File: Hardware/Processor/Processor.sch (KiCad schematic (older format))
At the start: 0 parts

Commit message: Started schematic capture for mcu dev board
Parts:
- added C? (x2): 10uF, symbol C
- added C?: 22uF, symbol C
- added C? (x17): 100nF, symbol C
- added C? (x7): 10nF, symbol C
- added C?: 4.7uF, symbol C
- added C?: 2.2uF, symbol C
- added D?: Zener, symbol D_Zener_ALT
- added J?: SWD, symbol CONN_02X05
- added L?: 2.2uH, symbol L
- added L?: 10uH, symbol L
- added R? (x3): 100k, symbol R
- added R?: 1R, symbol R
- added R?: 10k, symbol R
- added U?: ATSAM4E16E, symbol ATSAM4E16E
- added U?: TPS62162, symbol TPS6216
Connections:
- net labels added: +1V2, +3V3, +5V, AREF, GND, SWDCLK, SWDIO, TRACESWO, VDDPLL, ~P_GOOD, ~RST
- wire segments 0 -> 147
- no-connect marks 0 -> 3

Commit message: Changed buck regulator, added usb hw, added pio busses & net names
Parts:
- removed R?: 100k, symbol R
- removed U?: TPS62162, symbol TPS6216
- added C?: 4.5nF, symbol C
- added J?: USB_OTG, symbol USB_OTG
- added R?: 1M, symbol R
- added R? (x2): 0R, symbol R
- added TVS?: PRTR5V0U2X, symbol PRTR5V0U2X
- added U?: LM3671, symbol LM3671
- C?: value 10uF -> 4.7uF
- C?: value 22uF -> 10uF
- D?: value Zener -> 3.0V
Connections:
- net labels added: DD+, DD-, ERASE, PA0, PA1, PA10, PA11, PA12, PA13, PA14, PA15, PA16, PA17, PA18, PA19, PA2, PA20, PA21, PA22, PA23, PA24, PA25, PA26, PA27, PA28, PA29, PA3, PA30, PA31, PA4, PA5, PA6, PA7, PA8, PA9, PB0, PB1, PB13, PB14, PB2, PB3, PB4, PB5, PB6, PB7, PC0, PC1, PC10, PC11, PC12, PC13, PC14, PC15, PC16, PC17, PC18, PC19, PC2, PC20, PC21, PC22, PC23, PC24, PC25, PC26, PC27, PC28, PC29, PC3, PC30, PC31, PC4, PC5, PC6, PC7, PC8, PC9, PD0, PD1, PD10, PD11, PD12, PD13, PD14, PD15, PD16, PD17, PD18, PD19, PD2, PD20, PD21, PD22, PD23, PD24, PD25, PD26, PD27, PD28, PD29, PD3, PD30, PD31, PD4, PD5, PD6, PD7, PD8, PD9, PE0, PE1, PE2, PE3, PE4, PE5, PIOA, PIOB, PIOD, USBD+, USBD-, XIN, XOUT
- net labels removed: ~P_GOOD
- wire segments 147 -> 273
- no-connect marks 3 -> 4
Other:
- moved on the sheet: C?, D?, L?, R?

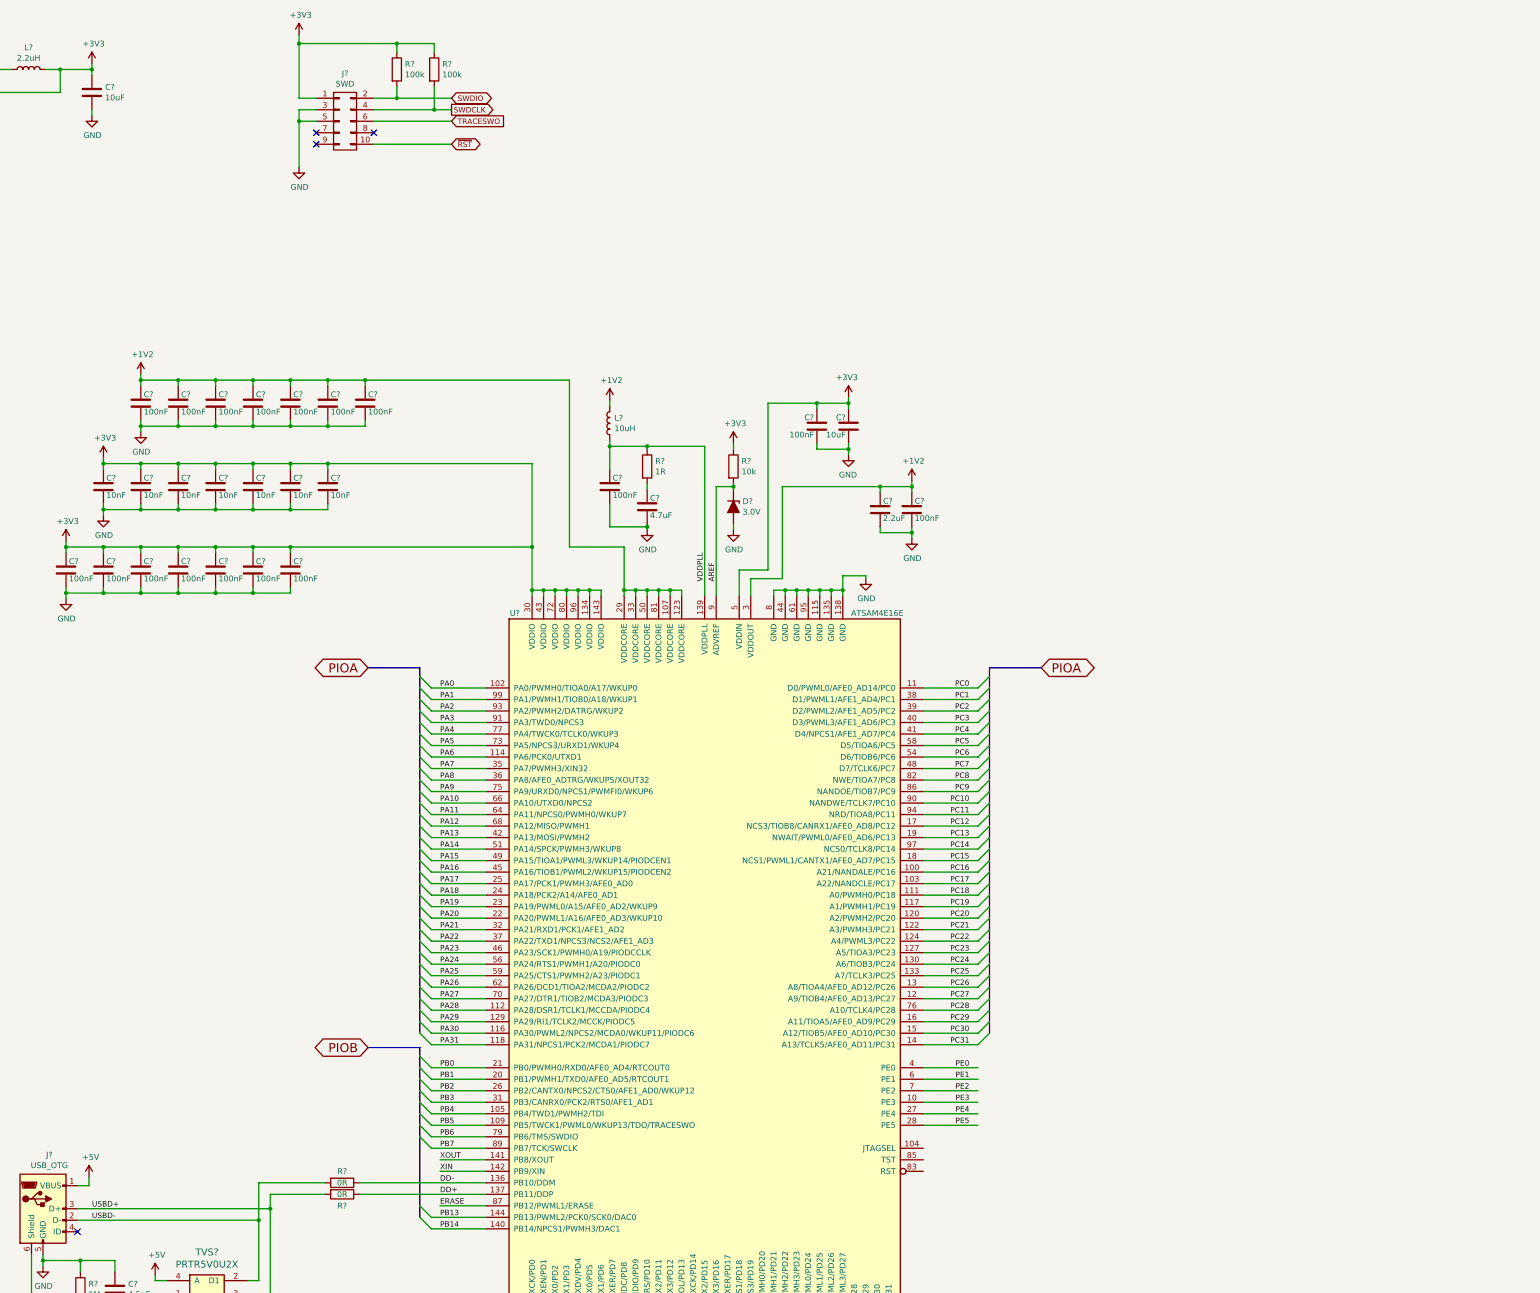
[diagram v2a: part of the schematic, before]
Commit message: Added leds
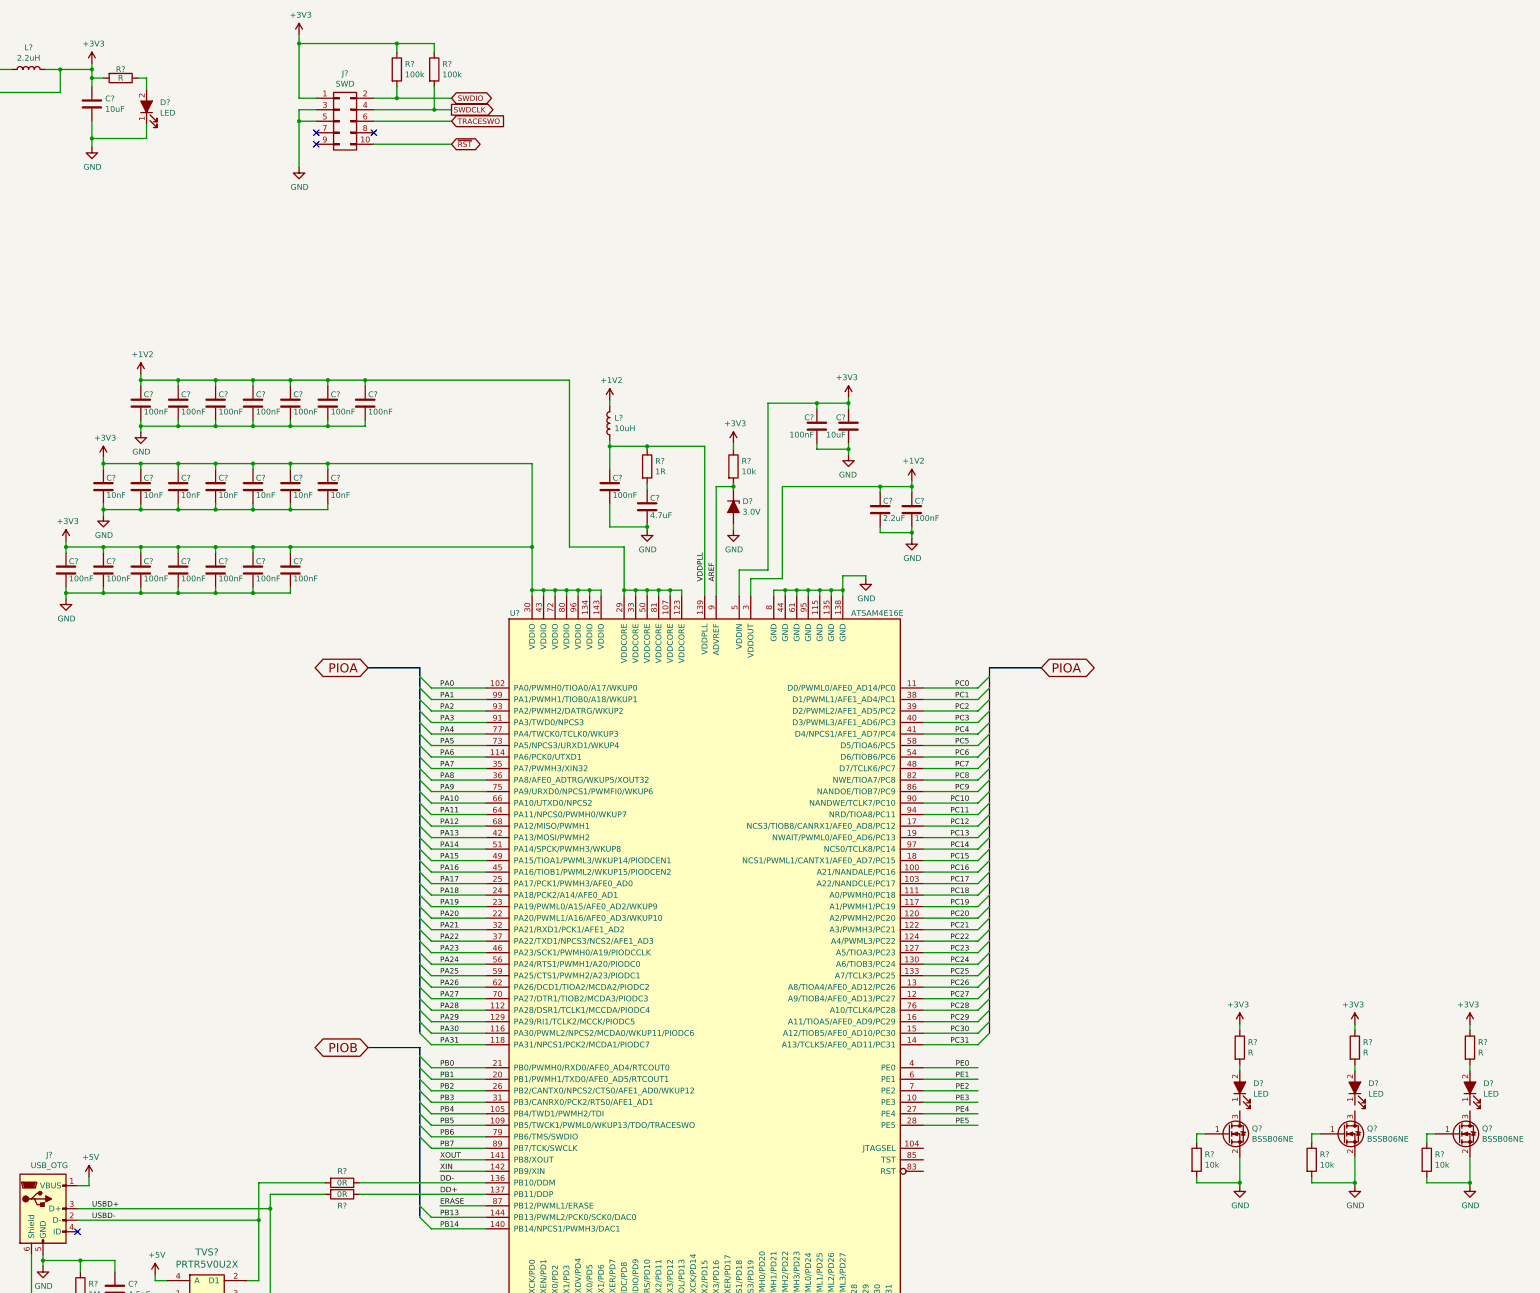
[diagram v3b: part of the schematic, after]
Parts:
- added D? (x4): LED, symbol LED_ALT
- added Q? (x3): BSSB06NE, symbol Q_NMOS_GSD
- added R? (x4): R, symbol R
- added R? (x3): 10k, symbol R
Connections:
- net +3V3: now also R?.1, R?.1, R?.1, R?.2
- net GND: now also D?.1 (K), Q?.2 (S), Q?.2 (S), Q?.2 (S), R?.2, R?.2, R?.2
- new net: Q?.1 (G), R?.1 (x3)
- new net: D?.2 (A), R?.2 (x3)
- new net: D?.2 (A), R?.1
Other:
- moved on the sheet: C?

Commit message: Finishing up draft MCU dev board schematic
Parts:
- removed R? (x2): 100k, symbol R
- added C? (x4): C, symbol C
- added C? (x2): 100nF, symbol C
- added J?: UART0, symbol CONN_01X04
- added J?: PIOA, symbol CONN_02X20
- added J? (x2): PIOD, symbol CONN_02X20
- added J?: PIOC, symbol CONN_02X20
- added J?: 5V, symbol CONN_01X02
- added JP?: 5V_SEL, symbol Jumper_NC_Dual
- added R? (x2): 10k, symbol R
- added R?: 0R, symbol R
- added TP?: ERASE, symbol TEST
- added TP?: TST, symbol TEST
- added TP?: JTAG_SEL, symbol TEST
- added TP?: U0_TXD, symbol TEST
- added TP?: U0_RXD, symbol TEST
- added TP? (x3): 5V, symbol TEST
- added U?: TXS0102, symbol TXS0102
- added Y?: 12MHz, symbol Crystal
- added Y?: 32.768kHz, symbol Crystal
- J?: value SWD -> JTAGICE3-SWD
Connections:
- net PB6 is gone; now on net SWDIO: U?.79 (PB6/TMS/SWDIO)
- net PB7 is gone; now on net SWDCLK: U?.89 (PB7/TCK/SWCLK)
- net TRACESWO is gone; now on net ~RST: J?.6 (P6)
- net +1V2: now also TP?.1
- net +3V3: now also J?.4 (P4), C?.1, J?.1 (P1), J?.1 (P1), J?.1 (P1), J?.1 (P1), J?.2 (P2), J?.2 (P2), J?.2 (P2), J?.2 (P2), J?.39 (P39), J?.39 (P39), J?.39 (P39), J?.39 (P39), J?.40 (P40), J?.40 (P40), J?.40 (P40), J?.40 (P40), R?.1, R?.1, TP?.1, U?.3 (VCCA), U?.6 (OE); no longer J?.1 (P1)
- net +5V: now also JP?.2, TP?.1; no longer J?.1 (VBUS)
- net ERASE: now also TP?.1
- net GND: now also J?.2 (P2), C?.2, C?.2, C?.2, C?.2, C?.2, C?.2, J?.1 (P1), J?.2 (P2), J?.3 (P3), J?.3 (P3), J?.3 (P3), J?.3 (P3), J?.37 (P37), J?.37 (P37), J?.37 (P37), J?.37 (P37), J?.38 (P38), J?.38 (P38), J?.38 (P38), J?.38 (P38), J?.4 (P4), J?.4 (P4), J?.4 (P4), J?.4 (P4), U?.2 (GND); no longer J?.3 (P3), J?.5 (P5)
- net PA0: now also J?.5 (P5)
- net PA1: now also J?.7 (P7)
- net PA11: now also J?.27 (P27)
- net PA12: now also J?.29 (P29)
- net PA13: now also J?.31 (P31)
- net PA14: now also J?.33 (P33)
- net PA15: now also J?.35 (P35)
- net PA16: now also J?.6 (P6)
- net PA17: now also J?.8 (P8)
- net PA18: now also J?.10 (P10)
- net PA19: now also J?.12 (P12)
- net PA2: now also J?.9 (P9)
- net PA20: now also J?.14 (P14)
- net PA21: now also J?.16 (P16)
- net PA22: now also J?.18 (P18)
- net PA23: now also J?.20 (P20)
- net PA24: now also J?.22 (P22)
- net PA25: now also J?.24 (P24)
- net PA26: now also J?.26 (P26)
- net PA27: now also J?.28 (P28)
- net PA28: now also J?.30 (P30)
- net PA29: now also J?.32 (P32)
- net PA3: now also J?.11 (P11)
- net PA30: now also J?.34 (P34)
- net PA31: now also J?.36 (P36)
- net PA4: now also J?.13 (P13)
- net PA5: now also J?.15 (P15)
- net PA6: now also J?.17 (P17)
- net PC0: now also J?.5 (P5)
- net PC1: now also J?.7 (P7)
- net PC10: now also J?.25 (P25)
- net PC11: now also J?.27 (P27)
- net PC12: now also J?.29 (P29)
- net PC13: now also J?.31 (P31)
- net PC14: now also J?.33 (P33)
- net PC15: now also J?.35 (P35)
- net PC16: now also J?.6 (P6)
- net PC17: now also J?.8 (P8)
- net PC18: now also J?.10 (P10)
- net PC19: now also J?.12 (P12)
- net PC2: now also J?.9 (P9)
- net PC20: now also J?.14 (P14)
- net PC21: now also J?.16 (P16)
- net PC22: now also J?.18 (P18)
- net PC23: now also J?.20 (P20)
- net PC24: now also J?.22 (P22)
- net PC25: now also J?.24 (P24)
- net PC26: now also J?.26 (P26)
- net PC27: now also J?.28 (P28)
- net PC28: now also J?.30 (P30)
- net PC29: now also J?.32 (P32)
- net PC3: now also J?.11 (P11)
- net PC30: now also J?.34 (P34)
- net PC31: now also J?.36 (P36)
- net PC4: now also J?.13 (P13)
- net PC5: now also J?.15 (P15)
- net PC6: now also J?.17 (P17)
- net PC7: now also J?.19 (P19)
- net PC8: now also J?.21 (P21)
- net PC9: now also J?.23 (P23)
- net PD0: now also J?.5 (P5), J?.5 (P5)
- net PD1: now also J?.7 (P7), J?.7 (P7)
- net PD10: now also J?.25 (P25), J?.25 (P25)
- net PD11: now also J?.27 (P27), J?.27 (P27)
- net PD12: now also J?.29 (P29), J?.29 (P29)
- net PD13: now also J?.31 (P31), J?.31 (P31)
- net PD14: now also J?.33 (P33), J?.33 (P33)
- net PD15: now also J?.35 (P35), J?.35 (P35)
- net PD16: now also J?.6 (P6), J?.6 (P6)
- net PD17: now also J?.8 (P8), J?.8 (P8)
- net PD18: now also J?.10 (P10), J?.10 (P10)
- net PD19: now also J?.12 (P12), J?.12 (P12)
- net PD2: now also J?.9 (P9), J?.9 (P9)
- net PD20: now also J?.14 (P14), J?.14 (P14)
- net PD21: now also J?.16 (P16), J?.16 (P16)
- net PD22: now also J?.18 (P18), J?.18 (P18)
- net PD23: now also J?.20 (P20), J?.20 (P20)
- net PD24: now also J?.22 (P22), J?.22 (P22)
- net PD25: now also J?.24 (P24), J?.24 (P24)
- net PD26: now also J?.26 (P26), J?.26 (P26)
- net PD27: now also J?.28 (P28), J?.28 (P28)
- net PD28: now also J?.30 (P30), J?.30 (P30)
- net PD29: now also J?.32 (P32), J?.32 (P32)
- net PD3: now also J?.11 (P11), J?.11 (P11)
- net PD30: now also J?.34 (P34), J?.34 (P34)
- net PD31: now also J?.36 (P36), J?.36 (P36)
- net PD4: now also J?.13 (P13), J?.13 (P13)
- net PD5: now also J?.15 (P15), J?.15 (P15)
- net PD6: now also J?.17 (P17), J?.17 (P17)
- net PD7: now also J?.19 (P19), J?.19 (P19)
- net PD8: now also J?.21 (P21), J?.21 (P21)
- net PD9: now also J?.23 (P23), J?.23 (P23)
- net SWDCLK: now also J?.1 (P1), R?.2; no longer J?.4 (P4)
- net SWDIO: now also J?.5 (P5); no longer J?.2 (P2)
- net XIN: now also C?.1, Y?.2
- net XOUT: now also C?.1, Y?.1
- net ~RST: now also U?.83 (RST); no longer J?.10 (P10)
- net JTAG_SEL: now reaches U?.104 (JTAGSEL)
- net JTAG_SEL: now also TP?.1
- net TST: now reaches U?.85 (TST)
- net TST: now also TP?.1
- net at Q?.3 (D): now also D?.1 (K) (x3)
- net PA10 renamed U0_TXD
- net U0_TXD: now also R?.2, TP?.1, U?.4 (A2)
- net PA7 renamed XIN32
- net XIN32: now also C?.1, Y?.1
- net PA8 renamed XOUT32
- net XOUT32: now also C?.1, Y?.2
- net PA9 renamed U0_RXD
- net U0_RXD: now also TP?.1, U?.5 (A1)
- net PB5 renamed SWO
- net SWO: now also R?.2
- new net: J?.3 (P3), R?.1
- new net +5V_UART: C?.1, J?.4 (P4), U?.7 (VCCB)
- new net 5V_EXT: J?.1 (P1), JP?.1
- new net UART_RXD: J?.2 (P2), U?.1 (B2)
- new net UART_TXD: J?.3 (P3), U?.8 (B1)
- new net VBUS: J?.1 (VBUS), JP?.3
- no-connect marks 4 -> 9
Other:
- moved on the sheet: C?, D?, J?, L?, Q?, R?, TVS?, U?

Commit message: Added default layout sheet. Finished schematic except pushbutton inputs
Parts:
- removed J?: PIOD, symbol CONN_02X20
- added D?: LED, symbol LED_ALT
- added J?: PIOB, symbol CONN_02X12
- added Q?: BSSB06NE, symbol Q_NMOS_GSD
- added R?: R, symbol R
- added R?: 10k, symbol R
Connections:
- net +3V3: now also J?.1 (P1), J?.2 (P2), J?.23 (P23), J?.24 (P24), R?.1
- net GND: now also J?.21 (P21), J?.22 (P22), J?.3 (P3), J?.4 (P4), Q?.2 (S), R?.2
- net PB0: now also J?.5 (P5)
- net PB1: now also J?.7 (P7)
- net PB13: now also J?.16 (P16)
- net PB14: now also J?.18 (P18)
- net PB2: now also J?.9 (P9)
- net PB3: now also J?.11 (P11)
- net PB4: now also J?.13 (P13)
- net PE0: now also Q?.1 (G), R?.1
- net PE1: now also Q?.1 (G), R?.1
- net PE2: now also Q?.1 (G), R?.1
- net PE3: now also Q?.1 (G), R?.1
- new net: D?.1 (K), Q?.3 (D)
- new net: D?.2 (A), R?.2
- no-connect marks 9 -> 18
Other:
- moved on the sheet: C?, D?, J?, JP?, L?, Q?, R?, TP?, TVS?, U?, Y?

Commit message: Added pushbutton to common lib & finished schematic
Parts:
- added C? (x2): 100nF, symbol C
- added R? (x2): 10k, symbol R
- added SW? (x3): ~RST, symbol SW_PUSH
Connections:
- net +3V3: now also R?.1, R?.1
- net GND: now also C?.2, C?.2, SW?.2, SW?.2, SW?.2
- net PE4: now also C?.1, R?.2, SW?.1
- net PE5: now also C?.1, R?.2, SW?.1
- net ~RST: now also SW?.1
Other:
- moved on the sheet: C?, D?, J?, L?, R?, U?
